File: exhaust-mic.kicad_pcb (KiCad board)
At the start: 4 copper layers, 72 x 55 mm, 131 parts, among them J1 JST_XH_6pol, J2 JST_XH_5pol_MicA, J3 JST_XH_5pol_MicB, J4 USB-C, J5 microSD_PushPush, J6 GPS_unbestueckt, J7 I2C_Erweiterung, Q1 SI2309CDS, Q3 2N7002, Q4 2N7002, SW1 RESET, SW2 BOOT, SW3 REC, SW4 MARK, U1 LM5164DDA, U2 NCP1117ST33, U3 LP5907MFX-3.3, U5 PCM1863DBT, U6 ESP32-S3-WROOM-1-N8R2, U7 DS3231SN, U8 SN65HVD230Q, Y1 24.576MHz

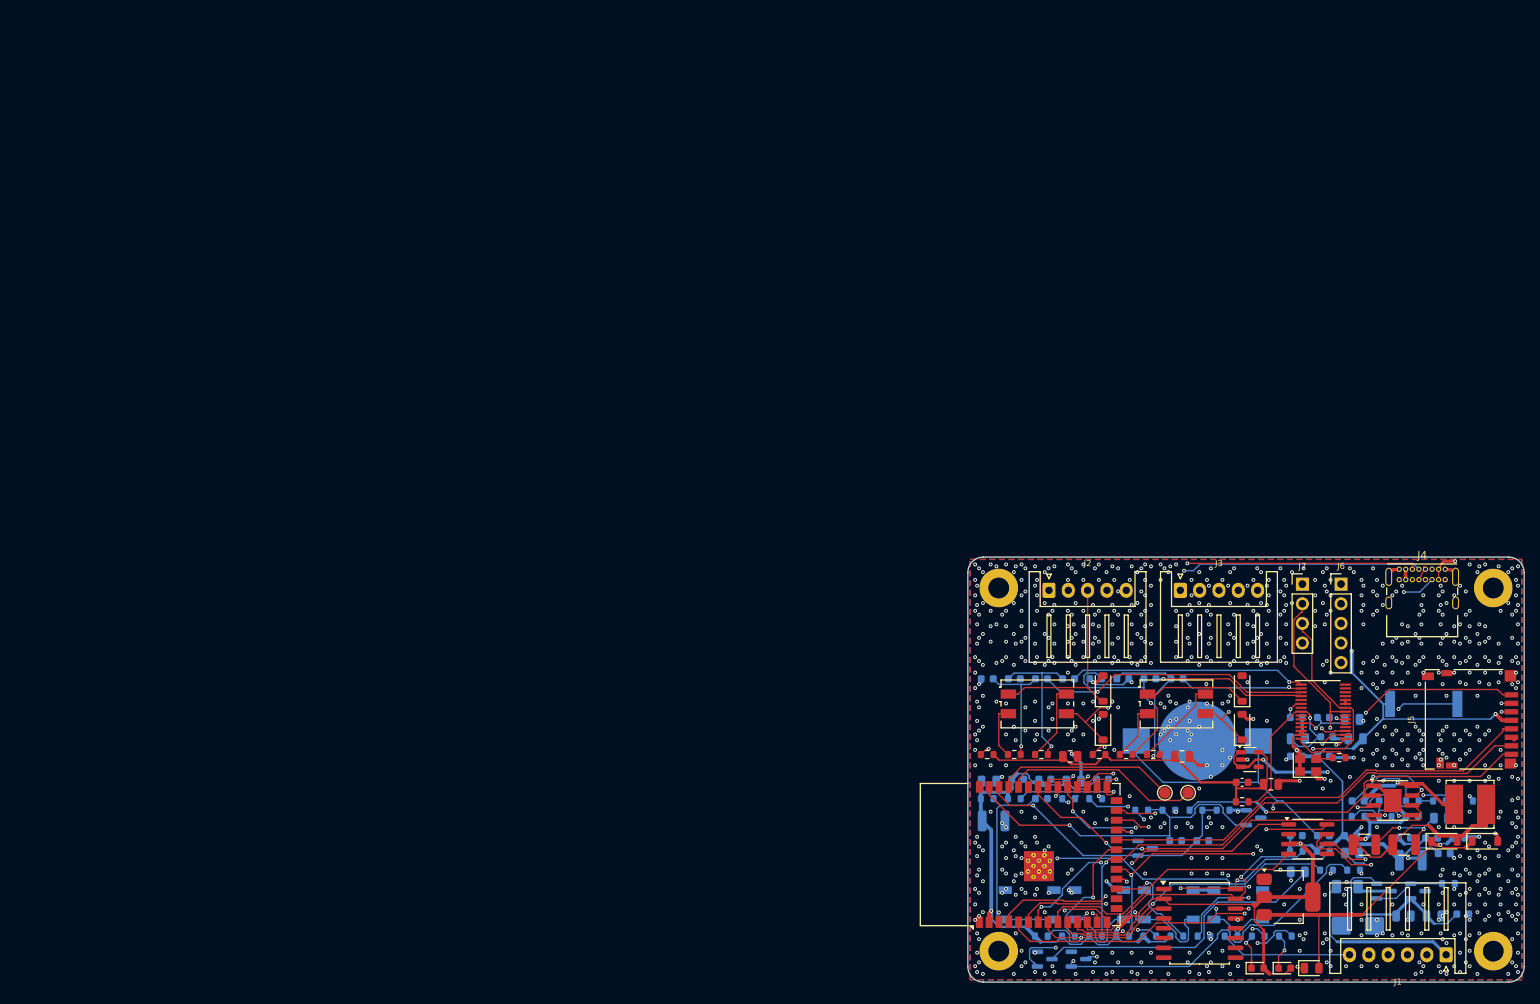
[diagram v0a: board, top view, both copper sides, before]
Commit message: Steckverbinder nach aussen drehen und Bauhoehe auf die Oberseite legen
Die Oeffnung der Kantenstecker liegt bei rot=0 auf +y, nicht auf -y. Der
Kommentar in build_pcb.py behauptete das Gegenteil, weshalb J1 bis J4 mit
der Oeffnung ins Platineninnere zeigten; beim GCT-USB4085 landete die
Kantenmarke 7,7 mm innen und die Buchse war unbenutzbar. Belege dafuer
stehen in den Footprints selbst: die JST-Horizontalumrisse haben die
Stiftaussparung hinten, USB4085 traegt eine Linie "PCB Edge" auf Dwgs.User.

Neue Anordnung nach Kevins Vorgaben:
- J1, J2 und J3 nebeneinander an der oberen Kante, Oeffnung nach aussen
- microSD 3,1 mm weiter nach innen: die Kartenspitze endet jetzt 0,5 mm
  vor der Kante statt 3,1 mm dahinter
- Knopfzelle, die vier Taster und der Piezo auf die Oberseite
- auf der Rueckseite bleibt nichts ueber 2,7 mm stehen (vorher 4,3 mm);
  dafuer sind U5, U7, U2, U3, U8 und die Serienglieder dorthin gewandert
- Platinengroesse unveraendert 72 x 55 mm

Dabei gefundene Fehler in den Werkzeugen:
- handroute.py und stitch.py setzten Vias ohne Blick auf die Kontur; zwei
  landeten ausserhalb der Platine. pcbgen.inside_outline() prueft jetzt
  acht Punkte auf dem Via-Rand gegen das Konturpolygon.
- cleanup.py entfernte lose Bahnenden pauschal und hob damit die offenen
  Verbindungen von 7 auf 9. Ein Segment quer durch eine gefuellte
  Masseflaeche traegt, auch wenn es an keinem Pad haengt. Jetzt wird
  nachgezaehlt und im Zweifel einzeln vorgegangen.
- widen_supply.py suchte die beanstandete Bahn ueber ein 0,005-mm-Raster
  auf Anfang, Ende und Mitte. KiCad meldet aber die Beruehrungsstelle, und
  0,005 mm daneben fiel sie in den falschen Eimer - ein Kurzschluss
  zwischen einer CAN_TX-Durchkontaktierung und einer 0,5 mm breiten
  +4V6-Bahn blieb so stehen. Jetzt Abstand Punkt zu Strecke.
- pcbgen liess das Feld Datasheet aus; das waren vier Paritaetsmeldungen.

Ergebnis: 0 DRC-Fehler, 0 ERC-Fehler, 7 offene Verbindungen (vier
Masseflaechen-Stuecke und drei Pads, 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
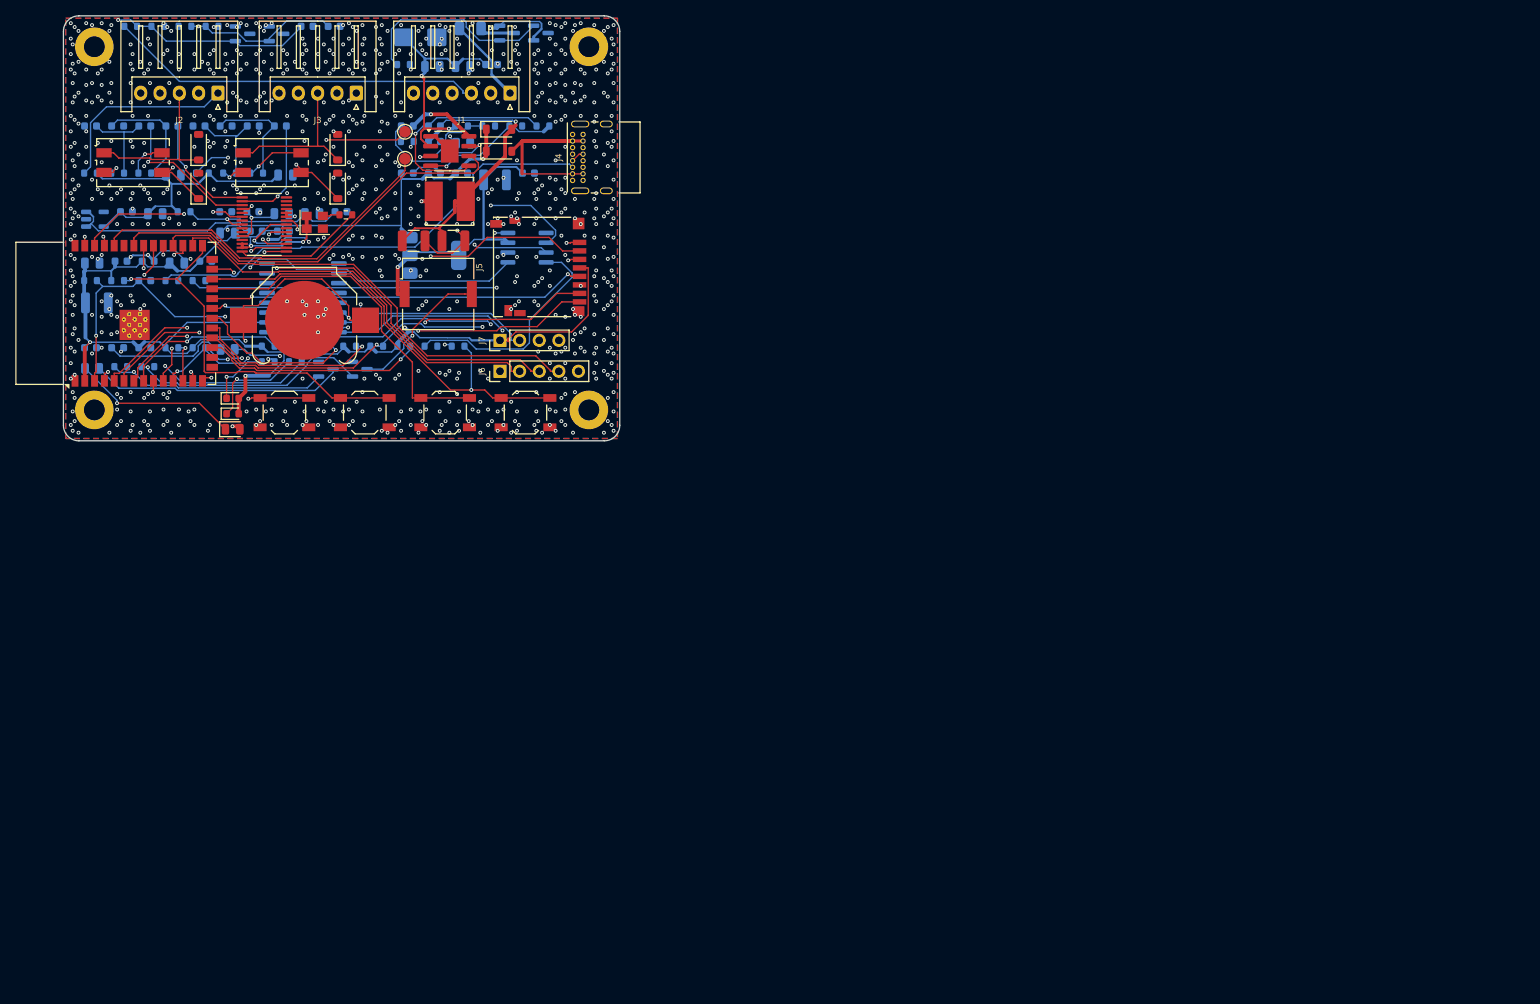
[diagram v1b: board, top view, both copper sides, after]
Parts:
- BT1, LS1, SW1, SW2, SW3, SW4: moved to F.Cu
- C14, C15, C20, C25, FB2, FB3, FB4, R20, R21, R22, R23, U2, U3, U7, U8: moved to B.Cu
- moved R1 171.8 mm to (44.0, 6.30)
- moved R54 169.1 mm to (7.42, 45.4)
- moved R53 169.1 mm to (3.71, 45.6)
- moved R55 169.1 mm to (10.9, 45.4)
- moved C52 168.3 mm to (10.5, 43.0)
- moved C50 168.3 mm to (3.50, 43.0)
- moved C51 168.3 mm to (7.01, 43.0)
- moved D2 167.2 mm to (46.2, 2.77)
- moved C1 167.0 mm to (47.7, 6.55)
- moved C2 167.0 mm to (51.7, 6.55)
- moved C3 167.0 mm to (55.4, 6.30)
- moved R9 165.6 mm to (8.71, 1.35)
- moved R12 165.6 mm to (19.2, 1.35)
- moved D5 165.6 mm to (23.2, 2.33)
- moved R10 165.6 mm to (12.2, 1.35)
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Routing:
- net CANL: track 20.1 -> 85.4 mm, vias 1 -> 2
- net Net-(LS1--): track 70.8 -> 18.4 mm, vias 2 -> 1
- net CANH: track 26.8 -> 76.5 mm, vias 1 -> 2
- net GND: track 71.9 -> 23.4 mm, vias 821 -> 810
- net CAN_RX: track 35.1 -> 66.5 mm, vias 0 -> 2
- net I2S_BCK: track 62.2 -> 32.2 mm
- net SD_D3: track 94.2 -> 64.6 mm
- net BTN_MARK: track 28.4 -> 58.0 mm, vias 2 -> 1
- net SD_CMD: track 84.4 -> 55.5 mm, vias 2 -> 3
- net VBAT12: track 79.5 -> 50.7 mm
- net PCM_INT: track 57.4 -> 28.8 mm, vias 3 -> 2
- net I2S_LRCK: track 59.7 -> 31.4 mm
- net SD_D2: track 84.4 -> 56.8 mm
- net BUZZ: track 74.7 -> 47.5 mm
- net UART0_TX: track 23.2 -> 45.9 mm, vias 0 -> 2
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
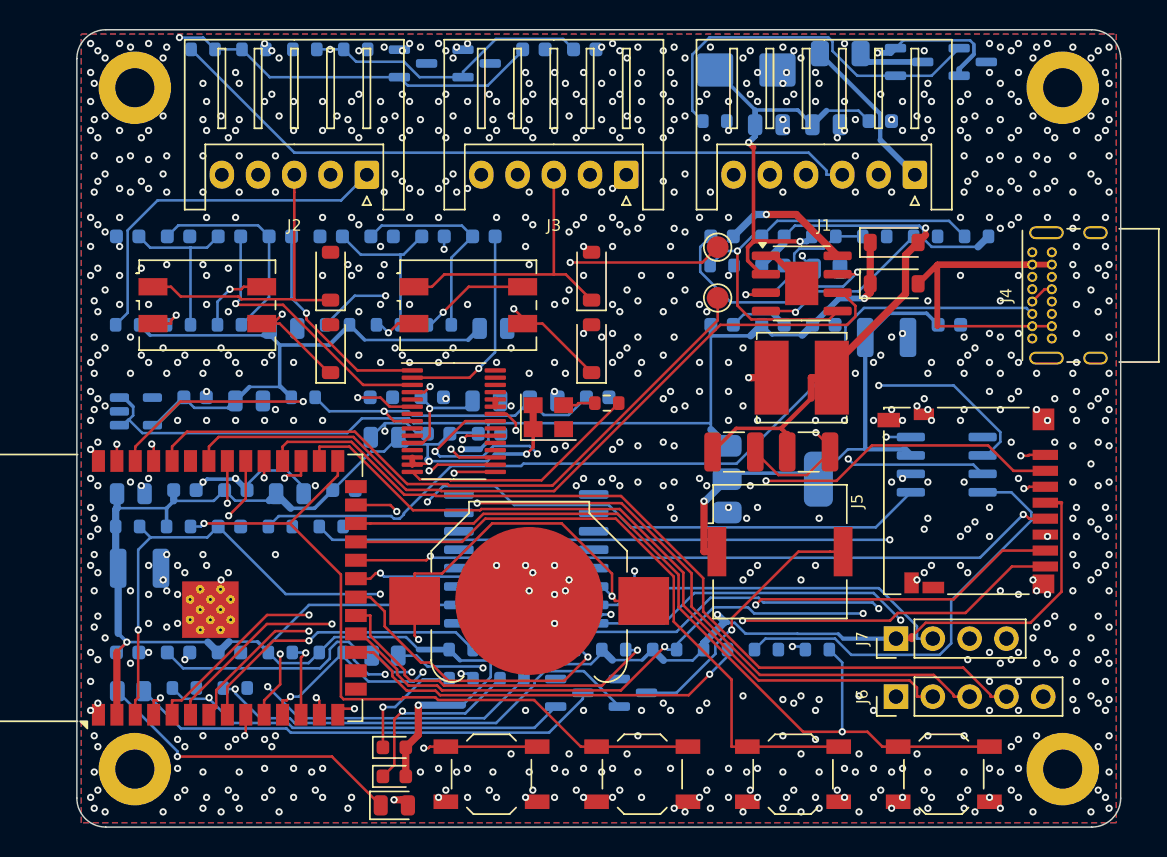
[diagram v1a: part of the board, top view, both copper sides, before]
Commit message: modified:   01-power.kicad_sch 	modified:   04-mcu.kicad_sch 	modified:   README.md 	modified:   docs/beschaffung.md 	modified:   docs/entwicklung.md 	modified:   exhaust-mic.kicad_pcb 	modified:   firmware/README.md 	modified:   firmware/main/CMakeLists.txt 	modified:   firmware/main/main.c 	modified:   firmware/main/pins.h 	new file:   firmware/main/zuendung.c 	new file:   firmware/main/zuendung.h 	modified:   firmware/tools/pins_aus_netzliste.py 	modified:   output/bilder/hauptplatine-bottom.png 	modified:   output/bilder/hauptplatine-top.png 	modified:   output/bom-mainboard.csv 	modified:   output/exhaust-mic-schaltplan.pdf 	modified:   output/hauptplatine-gerber.zip 	modified:   output/hauptplatine-oben.svg 	modified:   output/hauptplatine-pcb.pdf 	modified:   output/hauptplatine-pos.csv 	modified:   output/hauptplatine-unten.svg 	modified:   output/main.net
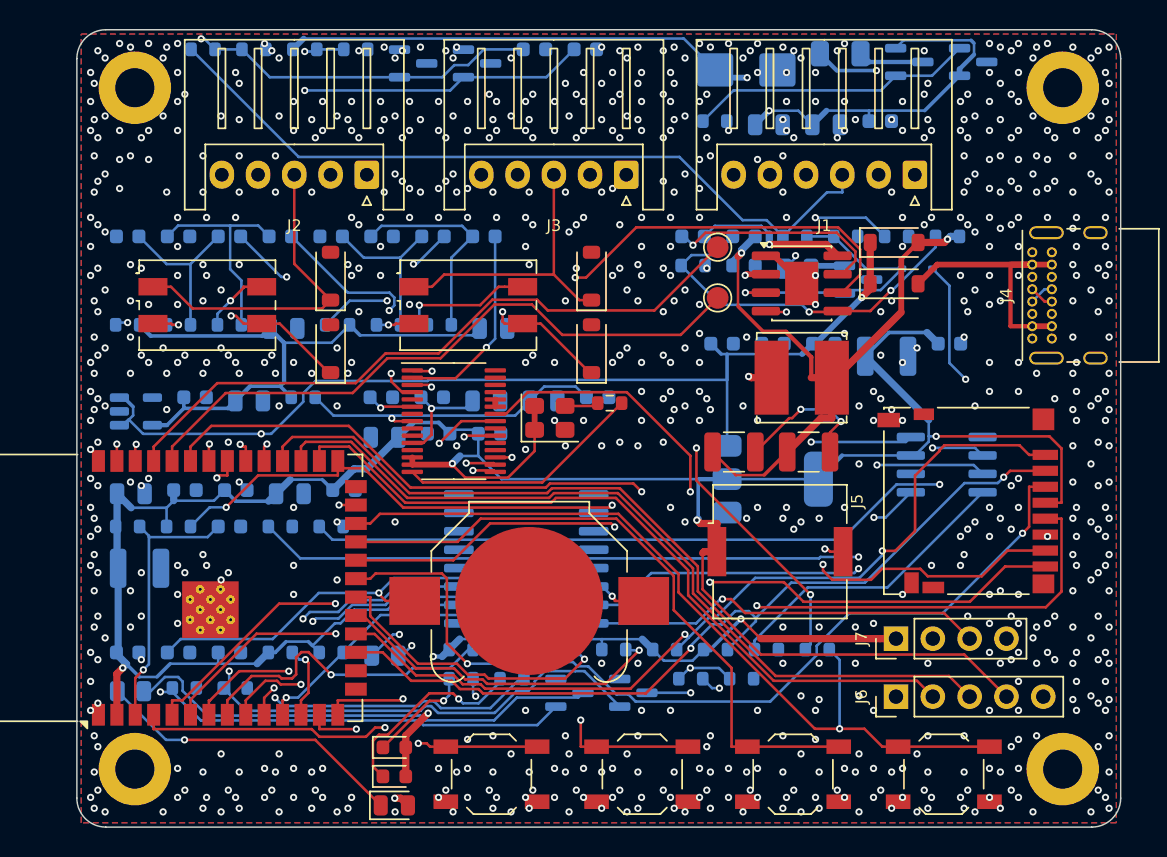
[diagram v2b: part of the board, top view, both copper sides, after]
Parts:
- added D7: BZX84C3V3, Package_TO_SOT_SMD:SOT-23, B.Cu at (53.9, 17.2)
- added D8: 1N4148WS, Diode_SMD:D_SOD-323, B.Cu at (58.0, 16.5)
- added R13: 10k, Resistor_SMD:R_0603_1608Metric, B.Cu at (42.3, 44.8)
- added R14: 10k, Resistor_SMD:R_0603_1608Metric, B.Cu at (45.9, 44.8)
- R2: value 1M -> 680k
- moved C4 2.00 mm to (42.5, 14.3)
- moved C5 2.00 mm to (46.0, 14.3)
- moved C8 2.00 mm to (46.0, 16.3)
- moved R2 2.00 mm to (49.5, 14.3)
- moved R3 2.00 mm to (53.0, 14.3)
- moved R4 2.00 mm to (56.5, 14.3)
- moved R5 2.00 mm to (60.1, 14.3)
- moved R6 2.00 mm to (42.5, 16.3)
- moved R7 2.00 mm to (49.7, 16.5)
- moved C11 1.30 mm to (55.9, 22.5)
- moved C10 1.30 mm to (48.0, 21.7)
- moved C12 1.30 mm to (60.2, 21.7)
- moved C13 1.30 mm to (51.5, 21.7)
- moved C9 1.30 mm to (44.5, 21.7)
- moved R24 0.20 mm to (36.8, 25.8)
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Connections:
- net Net-(U1-EN/UVLO) renamed /Versorgung/EN_UVLO
- R2 pad 1: VBAT12 -> IGN_IN
- U6 pad 35: unconnected-(U6-IO42-Pad35) -> PWR_HOLD
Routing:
- net PWR_HOLD: track 0.00 -> 54.0 mm, vias 0 -> 2
- net Net-(D8-A): track 0.00 -> 38.7 mm, vias 0 -> 2
- net VBAT12: track 50.7 -> 74.6 mm
- net USB_DP: track 82.5 -> 64.7 mm
- net GND: track 23.4 -> 6.86 mm, vias 810 -> 758
- net RTC_SQW: track 26.1 -> 42.1 mm, vias 1 -> 2
- net LED_REC: track 17.0 -> 32.7 mm
- net SD_CLK: track 49.1 -> 64.2 mm
- net CAN_RX: track 66.5 -> 54.6 mm
- net USB_DM: track 78.3 -> 67.7 mm
- net CANL: track 85.4 -> 75.2 mm
- net USB_VBUS: track 28.5 -> 18.4 mm
- net Net-(BT1-+): track 48.0 -> 38.5 mm, vias 3 -> 2
- net Net-(U8-Rs): track 29.9 -> 20.6 mm
- net /Versorgung/EN_UVLO: track 11.9 -> 20.4 mm
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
